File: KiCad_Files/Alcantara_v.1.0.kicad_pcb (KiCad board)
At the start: 4 copper layers, 105.4 x 36.8 mm, 90 parts, among them IC1 TLV809ED29DBZR, IC2 MAX17201G+T, IC3 TLV803EA30DCKR, J1 U_FL-R-SMT_10_, J2 142-0701-801, J3 142-0701-801, J4 USB_B_Micro, J5 PJS008U-3000-0, J8 53261-0527, Q1 MMSS8050-H-TP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

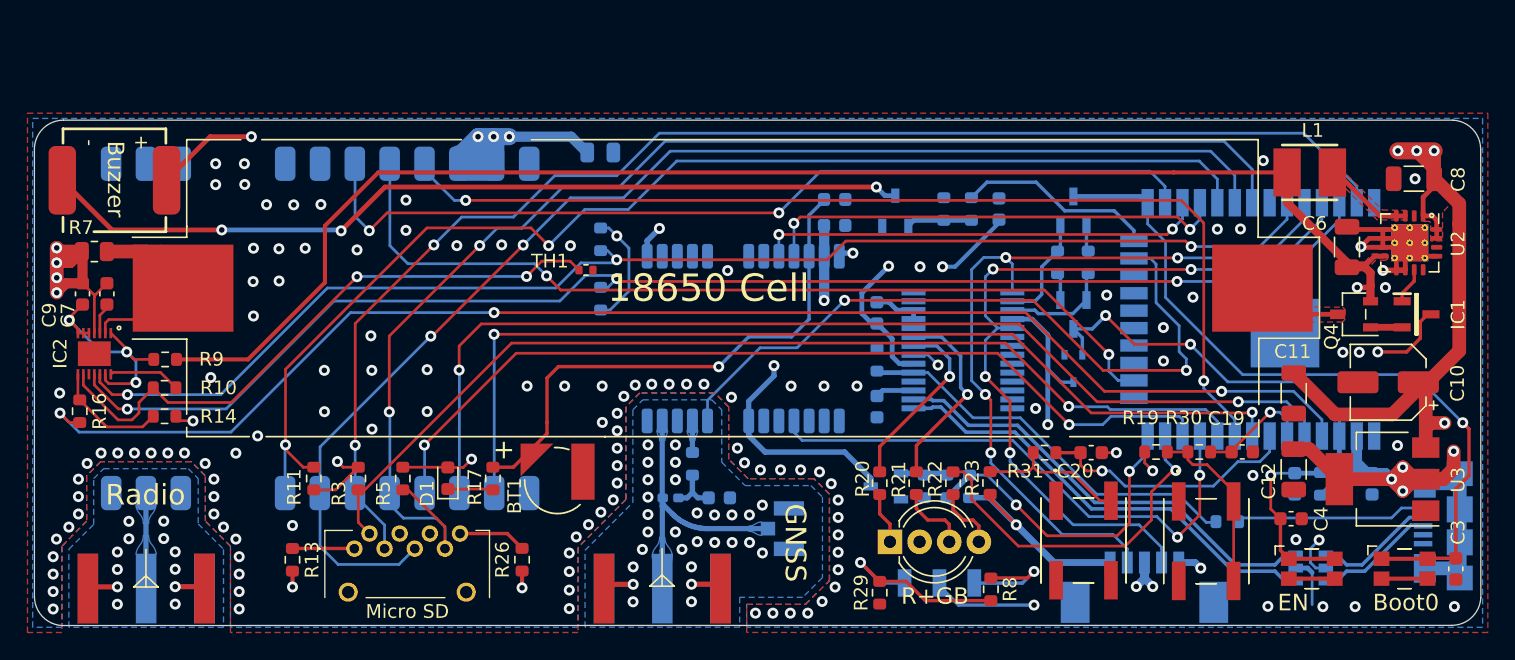
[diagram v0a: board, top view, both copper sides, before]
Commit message: Realocated and replaced components
Components where replaced because of the chip shortage, such as the 3.3 V Voltage regulator, the USB ESD protector and the SD Card holder.

The ESP32 has been rotated and moved closer to the center of the board, now having it's antenna positioned outside of the original board outline, providing better range for the Bluetooth and Wi-Fi.
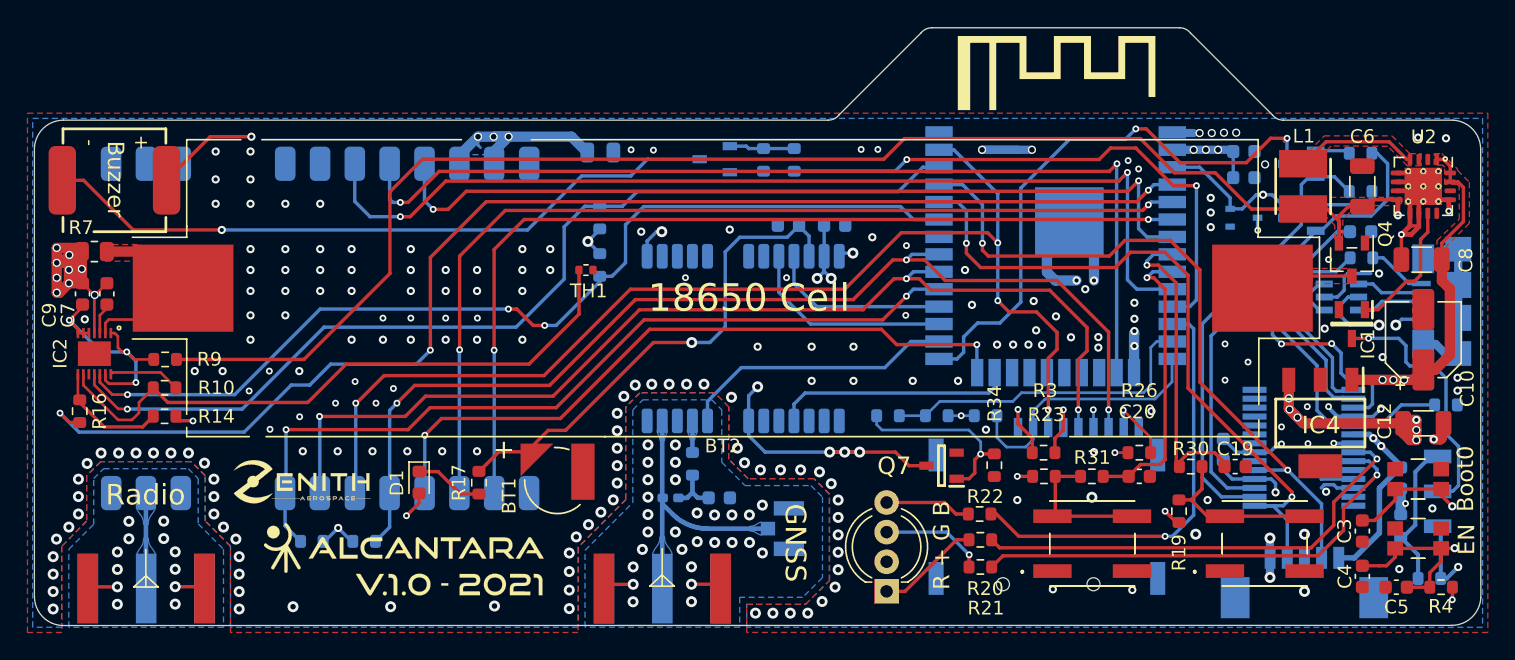
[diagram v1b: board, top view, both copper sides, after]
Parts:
- removed C11: 0.1uF, Capacitor_SMD:C_1206_3216Metric
- removed the G*** at (128.1, 32.1)
- removed U3: LD1117S33TR_SOT223, Package_TO_SOT_SMD:SOT-223-3_TabPin2
- removed U6: USBLC6-2SC6, Package_TO_SOT_SMD:SOT-23-6
- added G***: LOGO, LogosZenith:v.1.0 - 2021_1,6mm, F.Cu at (81.0, 63.1)
- added G***: LOGO, LogosZenith:Alcantarav+Logo_3,6mm, F.Cu at (77.7, 60.4)
- added IC4: TC1264-3.3VDB, SamacSys_Parts:SOT230P700X180-4N, F.Cu at (144.5, 51.3)
- added IC5: PESD2ETH-ADX, SamacSys_Parts:SOT95P275X110-6N, B.Cu at (146.1, 42.1)
- added REF**: 2.4_GHZ_Antenna_Left_Art, LogosZenith:2.4_GHZ_Antenna_Left_Art, F.Cu at (129.8, 28.2)
- C5, G***, Q7, R34, R4: moved to F.Cu
- J5: value PJS008U-3000-0 -> MEM2075-00-140-01-A; footprint SamacSys_Parts:PJS008U30000 -> SamacSys_Parts:MEM20750014001A; moved to B.Cu
- R11, R13, R5: moved to B.Cu
- R29: value 10 -> 100k; moved to B.Cu
- R8: value 10 -> 68k; moved to B.Cu
- moved R13 51.6 mm to (120.1, 50.7), turned to 180 degrees
- moved R3 50.0 mm to (124.3, 53.4), turned to 180 degrees
- moved J5 46.9 mm to (124.6, 59.3), turned to 180 degrees
- moved R26 45.7 mm to (131.3, 53.4), turned to 0 degrees
- moved R28 41.6 mm to (153.7, 50.0), turned to 0 degrees
- moved C17 40.0 mm to (150.4, 55.3), turned to 270 degrees
- moved G*** 38.8 mm to (70.6, 55.6), turned to 0 degrees
- moved R29 38.3 mm to (150.4, 58.8), turned to 270 degrees
- moved C18 37.5 mm to (147.4, 37.3), turned to 180 degrees
- moved S6 36.9 mm to (153.1, 56.3), turned to 90 degrees
- moved R8 32.0 mm to (152.5, 62.6), turned to 0 degrees
- moved U7 25.8 mm to (143.3, 53.1), turned to 90 degrees
- moved C2 25.3 mm to (138.9, 31.5), turned to 0 degrees
- moved C1 24.2 mm to (138.9, 33.4), turned to 0 degrees
- moved C16 24.0 mm to (137.4, 53.2)
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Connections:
- MOD1 pad 10: SDCARD_NSS -> RADIO_RXEN
- MOD1 pad 11: GPS_EXTINT -> BUZZER
- MOD1 pad 12: RADIO_NRST -> RGB_LED_B
- MOD1 pad 13: RGB_LED_B -> GPS_ON_OFF
- MOD1 pad 14: GPS_ON_OFF -> SDCARD_NSS
- MOD1 pad 23: GPS_RESET -> GPS_EXTINT
- MOD1 pad 24: BUZZER -> RADIO_NRST
- MOD1 pad 26: RADIO_RXEN -> GPS_RESET
- MOD1 pad 6: BUTTON_1 -> RADIO_DIO1
- MOD1 pad 7: BUTTON_2 -> RADIO_DIO2
- MOD1 pad 8: RADIO_DIO1 -> BUTTON_1
- MOD1 pad 9: RADIO_DIO2 -> BUTTON_2
- R13 pad 1: Net-(J5-Pad1) -> SDCARD_NSS
- R26 pad 2: Net-(J5-Pad8) -> Net-(J5-PadP8)
- R3 pad 2: SDCARD_NSS -> Net-(J5-PadP1)
- S2 pad 3: Net-(S2-Pad3) -> Net-(R23-Pad1)
- S6 pad 2: Net-(R29-Pad2) -> /Power Management/Pack
- S6 pad 3: /Power Management/Pack -> Net-(R29-Pad2)
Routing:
- net SDCARD_NSS: track 74.9 -> 19.5 mm, vias 1 -> 0
- net +5V: track 212.1 -> 168.5 mm, vias 10 -> 9
- net IO0: track 54.4 -> 90.8 mm, vias 1 -> 3
- net GPS_RESET: track 52.0 -> 20.1 mm, vias 2 -> 0
- net Net-(IC1-Pad3): track 50.0 -> 18.6 mm, vias 2 -> 1
- net RADIO_NSS: track 90.1 -> 60.5 mm
- net GAUGE_SCL: track 101.0 -> 72.6 mm, vias 3 -> 1
- net BUZZER: track 14.5 -> 41.4 mm, vias 0 -> 2
- net FTDI_RTS: track 7.89 -> 34.6 mm
- net +3V3: track 100.6 -> 74.1 mm, vias 16 -> 28
- net FTDI_DTR: track 8.11 -> 32.9 mm
- net GAUGE_SDA: track 95.7 -> 71.0 mm
- net GPS_EXTINT: track 40.0 -> 17.4 mm, vias 2 -> 0
- net USB_D+: track 33.1 -> 10.8 mm
- net GND: track 71.3 -> 92.5 mm, vias 133 -> 224
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- added copper zone on In2.Cu, net +3V3
- added copper zone on B.Cu, net +5V
- added copper zone on In1.Cu, net GND
- added copper zone on F.Cu, net Net-(BT2-Pad2)
- removed copper zone on In1.Cu, net +3V3
- removed copper zone on In2.Cu, net GND
- removed copper zone on B.Cu, net Net-(R18-Pad2)
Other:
- board size 105.4 x 36.8 mm -> 105.4 x 43.6 mm
- rule via_min_drill: 0.3 -> 0.2
- board text added: "R + G B"
- board text removed: "Micro-B"
- board text removed: "R+GB"
